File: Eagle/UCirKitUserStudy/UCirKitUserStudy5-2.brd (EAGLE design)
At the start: 83.8 x 94.3 mm, 30 parts, among them IC1 74595DIL16-OVAL-PIN, IC2 LM35TO92-EXPANDED-OVAL-PIN

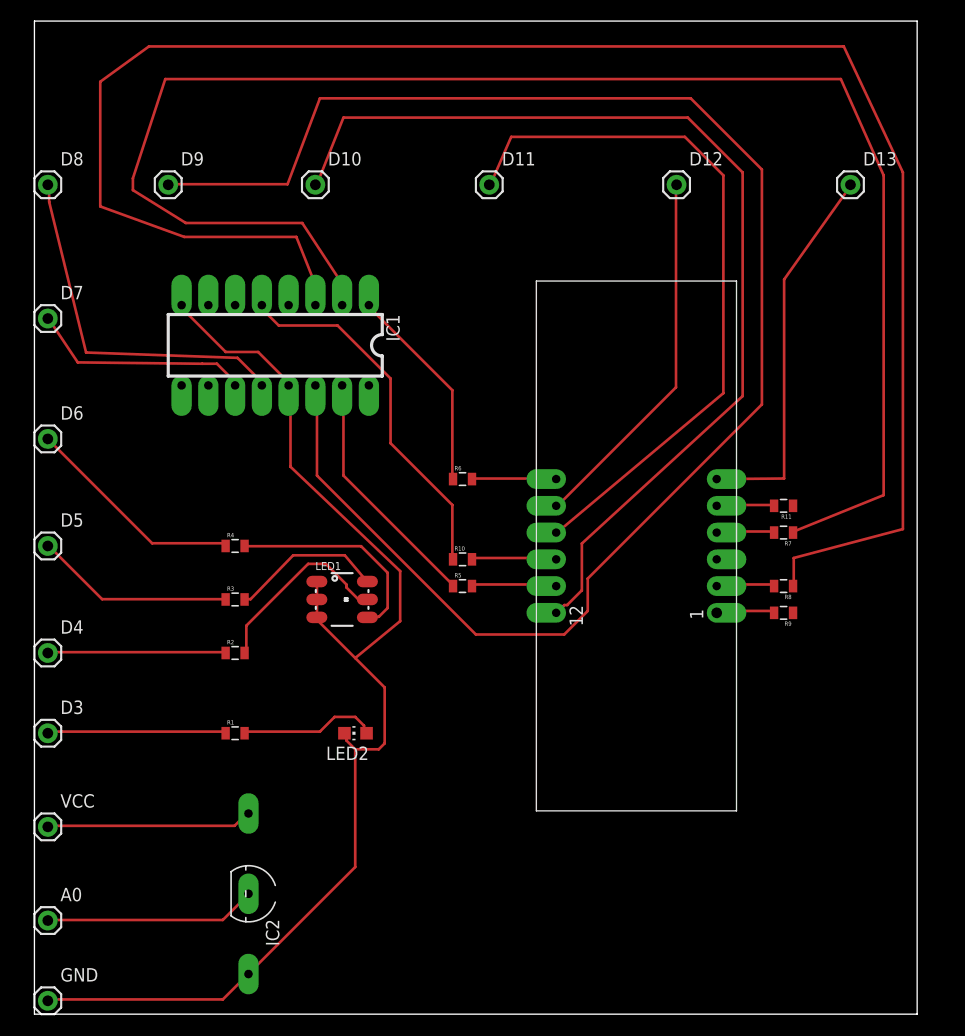
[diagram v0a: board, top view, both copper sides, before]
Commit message: UCirKitUserStudy4-2 and UCirKitUserStudy5-2 introduces 90 degree male headers for jumper wires
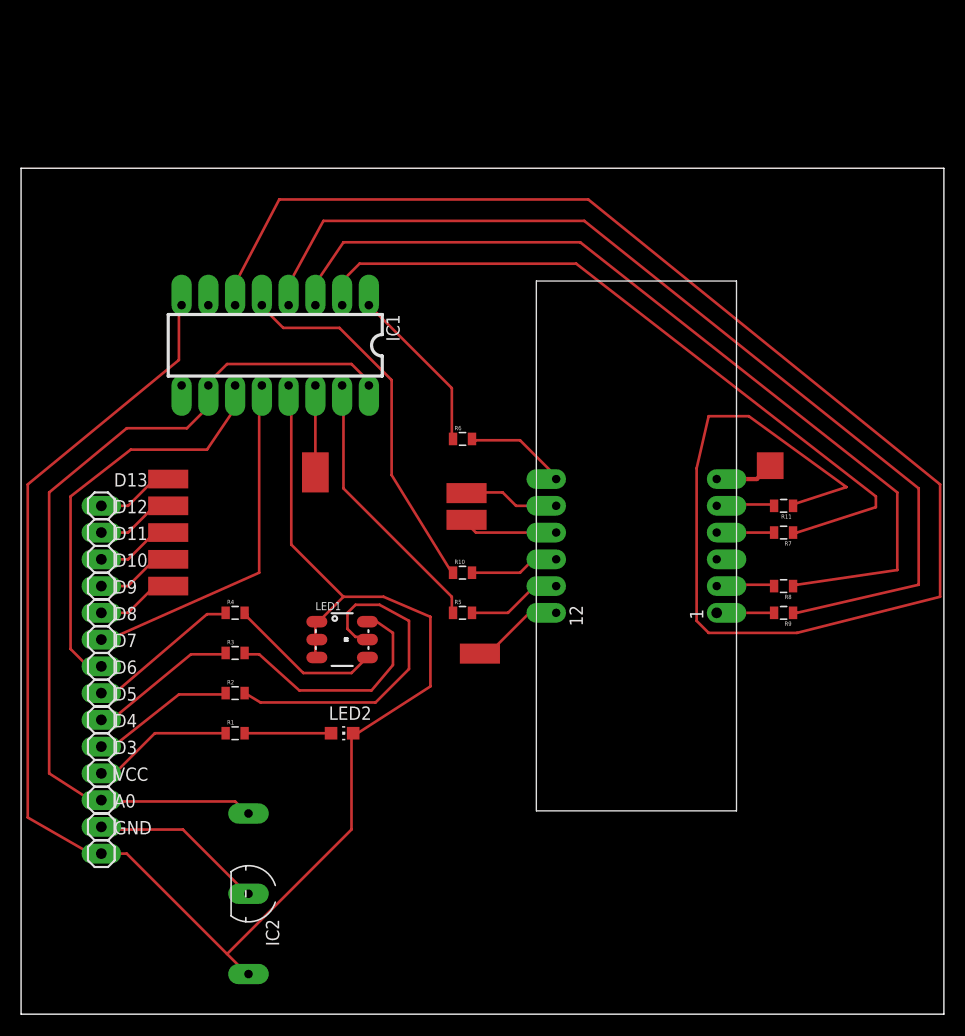
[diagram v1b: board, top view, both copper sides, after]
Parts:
- A0, D10, D11, D12, D13, D3, D4, D5, D6, D7, D8, D9, GND, VCC: device SparkFun-Connectors:1X01 -> SparkFun-Connectors:1X01_OVAL_PIN
- moved D13 77.4 mm to (6.35, 48.3)
- moved D12 63.8 mm to (6.35, 45.7)
- moved D11 51.2 mm to (6.35, 43.2)
- moved D8 43.5 mm to (6.35, 35.6)
- moved D10 43.2 mm to (6.35, 40.6)
- moved D9 41.1 mm to (6.35, 38.1)
- moved D7 33.4 mm to (6.35, 33.0)
- moved D6 24.7 mm to (6.35, 30.5)
- moved D5 17.3 mm to (6.35, 27.9)
- moved GND 14.9 mm to (6.35, 15.2)
- moved A0 10.2 mm to (6.35, 17.8)
- moved D4 10.2 mm to (6.35, 25.4)
- moved D3 6.35 mm to (6.35, 22.9)
- moved R4 6.35 mm to (19.1, 38.1)
- moved VCC 5.68 mm to (6.35, 20.3)
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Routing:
- net G: track 0.00 -> 158.4 mm
- net D9: track 155.1 -> 13.8 mm
- net E: track 0.00 -> 95.7 mm
- net D: track 170.0 -> 85.0 mm
- net D10: track 96.7 -> 14.1 mm
- net C: track 150.8 -> 70.5 mm
- net VCC: track 19.6 -> 84.7 mm
- net D11: track 68.0 -> 15.5 mm
- net GND: track 114.9 -> 161.5 mm
- net D13: track 36.3 -> 11.7 mm
- net D12: track 35.3 -> 15.5 mm
- net D7: track 21.3 -> 39.5 mm
- net N$8: track 18.2 -> 32.1 mm
- net N$9: track 14.6 -> 22.5 mm
- net D6: track 21.1 -> 14.6 mm
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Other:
- board size 83.8 x 94.3 mm -> 87.6 x 80.3 mm
